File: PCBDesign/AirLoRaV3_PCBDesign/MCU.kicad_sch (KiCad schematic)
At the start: 46 parts, among them IC1 BALFHB-WL-05D3, J2 SMA-J-P-H-ST-EM1, SW1 SW_Push, U3 BGS12WN6E6327, U6 STM32WLE5JCIx, Y1 NX2012SA 32.768KHz

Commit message: Updated Schematic
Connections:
- no-connect marks 27 -> 28
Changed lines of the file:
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@@
+	)
+	(no_connect
+		(at 234.95 154.94)
 	)
 	(no_connect

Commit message: Update circiut
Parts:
- removed J2: SMA-J-P-H-ST-EM1, SMA-J-P-H-ST-EM1:SAMTEC_SMA-J-P-H-ST-EM1, symbol SMA-J-P-H-ST-EM1:SMA-J-P-H-ST-EM1
- added J2: Conn_Coaxial, Connector_Coaxial:U.FL_Molex_MCRF_73412-0110_Vertical, symbol Connector:Conn_Coaxial
- C10: renamed from C8; footprint (none) -> Capacitor_SMD:C_0603_1608Metric
- C11: renamed from C9; footprint (none) -> Capacitor_SMD:C_0603_1608Metric
- C12: renamed from C10; footprint (none) -> Capacitor_SMD:C_0603_1608Metric
- C13: renamed from C11; footprint (none) -> Capacitor_SMD:C_0603_1608Metric
- C14: renamed from C12; footprint (none) -> Capacitor_SMD:C_0603_1608Metric
- C15: renamed from C13; footprint (none) -> Capacitor_SMD:C_0603_1608Metric
- C16, C17, C18, C19, C20, C21, C22, C23, C24, C25, C26, C27, C28, C29, C30, C31, C32, C33, C34, C35, C36, C37, C38, C39, C40: footprint (none) -> Capacitor_SMD:C_0603_1608Metric
- C9: renamed from C7; footprint (none) -> Capacitor_SMD:C_0603_1608Metric
- IC1: footprint BALFHBWL05D3 -> footprint:BALFHBWL05D3
- L2, L4, L5: footprint (none) -> Inductor_SMD:L_0603_1608Metric
- L3: footprint (none) -> Inductor_SMD:L_6.3x6.3_H3
- R7: renamed from R1; footprint (none) -> Resistor_SMD:R_0603_1608Metric
- R8: renamed from R2; footprint (none) -> Resistor_SMD:R_0603_1608Metric
- R9: renamed from R3; footprint (none) -> Resistor_SMD:R_0603_1608Metric
- SW1: footprint (none) -> Button_Switch_SMD:SW_Push_SPST_NO_Alps_SKRK
- U3: footprint Package_LGA:Infineon_PG-TSNP-6-10_0.7x1.1mm_0.7x1.1mm_P0.4mm -> footprint:BGS12SN6E6327XTSA1
- U4: renamed from U6; LCSC (none) -> C1121847; MFR (none) -> STM32WLE5CBU6
- XTAL1: footprint NT2016SA-32M-END4263A_NDK -> footprint:NT2016SA-32M-END4263A_NDK
- Y1: footprint (none) -> footprint:XTAL_NX2012SA-32.768K-STD-MUB-1
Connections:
- net GND: now also J2.1 (In)
- net at C9.2, L2.2: now also J2.2 (Ext)
- net PA6: now reaches U4.F4 (PA6)
- net PA7: now reaches U4.H3 (PA7)
- net PA4: now reaches U4.J1 (PA4)
- net PA5: now reaches U4.J2 (PA5)
- no-connect marks 28 -> 24

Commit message: Update PCB layout
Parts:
- added H1, H2, H3, H4: MountingHole_Pad, MountingHole:MountingHole_3mm_Pad_Via, symbol Mechanical:MountingHole_Pad
- L3: footprint Inductor_SMD:L_6.3x6.3_H3 -> Capacitor_SMD:C_0603_1608Metric_Pad1.08x0.95mm_HandSolder
- SW1: footprint Button_Switch_SMD:SW_Push_SPST_NO_Alps_SKRK -> Button_Switch_SMD:SW_Push_1P1T_NO_Vertical_Wuerth_434133025816
- renumbered R7 to R10, R8 to R11, R9 to R12
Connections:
- net GND: now also J2.2 (Ext), H1.1, H2.1, H3.1, H4.1; no longer J2.1 (In)
- net at C9.2, L2.2: now also J2.1 (In); no longer J2.2 (Ext)
- net PA12: now reaches U4.A9 (PA12)
- net PA11: now reaches U4.B9 (PA11)
- net PB2: now reaches U4.D8 (PB2)
- net PA8: now reaches U4.J3 (PA8)
- no-connect marks 24 -> 20
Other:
- moved on the sheet: J2

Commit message: Update schematic
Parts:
- removed C17: 68pF, Capacitor_SMD:C_0603_1608Metric, symbol Device:C
- removed C23: 47pF, Capacitor_SMD:C_0603_1608Metric, symbol Device:C
- removed C29, C36, C39: 100nF, Capacitor_SMD:C_0603_1608Metric, symbol Device:C
- removed C31, C33: 10pF, Capacitor_SMD:C_0603_1608Metric, symbol Device:C
- removed C35: 4.7uF, Capacitor_SMD:C_0603_1608Metric, symbol Device:C
- removed L5: 1400R 1GHz, Inductor_SMD:L_0603_1608Metric, symbol Device:L
- removed U4: STM32WLE5JCIx, Package_BGA:ST_UFBGA-73_5x5mm_Layout9x9_P0.5mm, symbol MCU_ST_STM32WL:STM32WLE5JCIx
- removed XTAL1: NT2016SA-32M-END4263A, footprint:NT2016SA-32M-END4263A_NDK, symbol NT2016SA-32M-:NT2016SA-32M-END4263A
- added C18: 0.47uF, Capacitor_SMD:C_0603_1608Metric, symbol Device:C
- added C27: 4.7uF, Capacitor_SMD:C_0603_1608Metric, symbol Device:C
- added C28: 100nF, Capacitor_SMD:C_0603_1608Metric, symbol Device:C
- added J3: LED, Connector_JST:JST_XA_B02B-XASK-1-A_1x02_P2.50mm_Vertical, symbol Connector:Conn_01x02_Pin
- added Q1: S8050, Package_TO_SOT_SMD:SOT-23, symbol Transistor_BJT:S8050
- added R13: 1K, Resistor_SMD:R_0603_1608Metric, symbol Device:R
- added U4: STM32WLE5CCUx, Package_DFN_QFN:QFN-48-1EP_7x7mm_P0.5mm_EP5.6x5.6mm, symbol MCU_ST_STM32WL:STM32WLE5CCUx
- added X1: NX2016SA-32MHZ, footprint:NX2016SA_NDK, symbol NX2016SA-32MHZ:NX2016SA-32MHZ-EXS00A-CS06654
- C16: renamed from C32; value 5.1pF -> 6.8pF
- C22: renamed from C34; value 10pF -> 6.8pF
- IC1: value BALFHB-WL-05D3 -> BALFHB-WL-02D3
- R12: value 220 -> 10K
- renumbered C21 to C17, C16 to C19, C18 to C20, C19 to C21, C22 to C23, C26 to C24, C28 to C25, C30 to C26, C20 to C29, C24 to C30, C25 to C31, C27 to C32, C37 to C33, C38 to C34, C40 to C35
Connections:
- net XTA is gone; now on net GND: C22.2
- net +3.3V: now also U4.11 (VDD), U4.37 (VBAT), U4.44 (VDD); no longer C33.1
- net GND: now also C12.1, C14.1, R12.1, C18.2, C27.2, C28.2, Q1.1 (E), U4.48 (VSSSMPS), U4.49 (VSS), X1.2, X1.4; no longer C12.2, C14.2
- net T_SWCLK: now also U4.42 (PA14)
- net T_SWDIO: now also U4.36 (PA13)
- net VDDPA: now also U4.25 (VDDPA); no longer C21.1, C35.1, L3.1
- net at IC1.A2 (RFI_N_OUT): now also U4.21 (RFI_N)
- net at IC1.A3 (RFI_P_OUT): now also U4.20 (RFI_P)
- net at C16.2: now also U4.26 (OSC_IN), X1.1
- net at R11.1: now also U4.38 (PC13)
- net at C23.2, Y1.1: now also U4.40 (PC15)
- net at C19.2, Y1.2: now also U4.39 (PC14)
- net at R10.2, U3.4 (VDD): now also C12.2, C14.2; no longer C12.1, C14.1
- net at C22.1: now also U4.27 (OSC_OUT), X1.3; no longer R12.2
- net at C17.2: now also U4.23 (RFO_HP)
- net at C20.2, SW1.2: now also U4.18 (NRST)
- net at L3.2: now also U4.47 (VLXSMPS)
- net VREF+: no longer names the net of C25.1, C26.1, L4.2
- net VREF+: now also U4.41 (VDDA)
- new net: R12.2, U4.19 (PH3)
- new net: R13.1, U4.8 (PA1)
- new net: J3.1 (Pin_1), Q1.3 (C)
- new net: Q1.2 (B), R13.2
- new net +5V: J3.2 (Pin_2)
- new net SCL1: U4.4 (PB6)
- new net SDA1: U4.5 (PB7)
- new net VDDRF: C27.1, C28.1, C33.1, U4.28 (VDDRF), U4.46 (VDDSMPS)
- new net VDDRF1V55: C18.1, C21.1, C35.1, L3.1, U4.29 (VDDRF1V55), U4.45 (VFBSMPS)
- no-connect marks 20 -> 24
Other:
- note added: "LED"
- moved on the sheet: C10, C11, C12, C13, C14, C15, C16, C17, C19, C22, C23, C25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

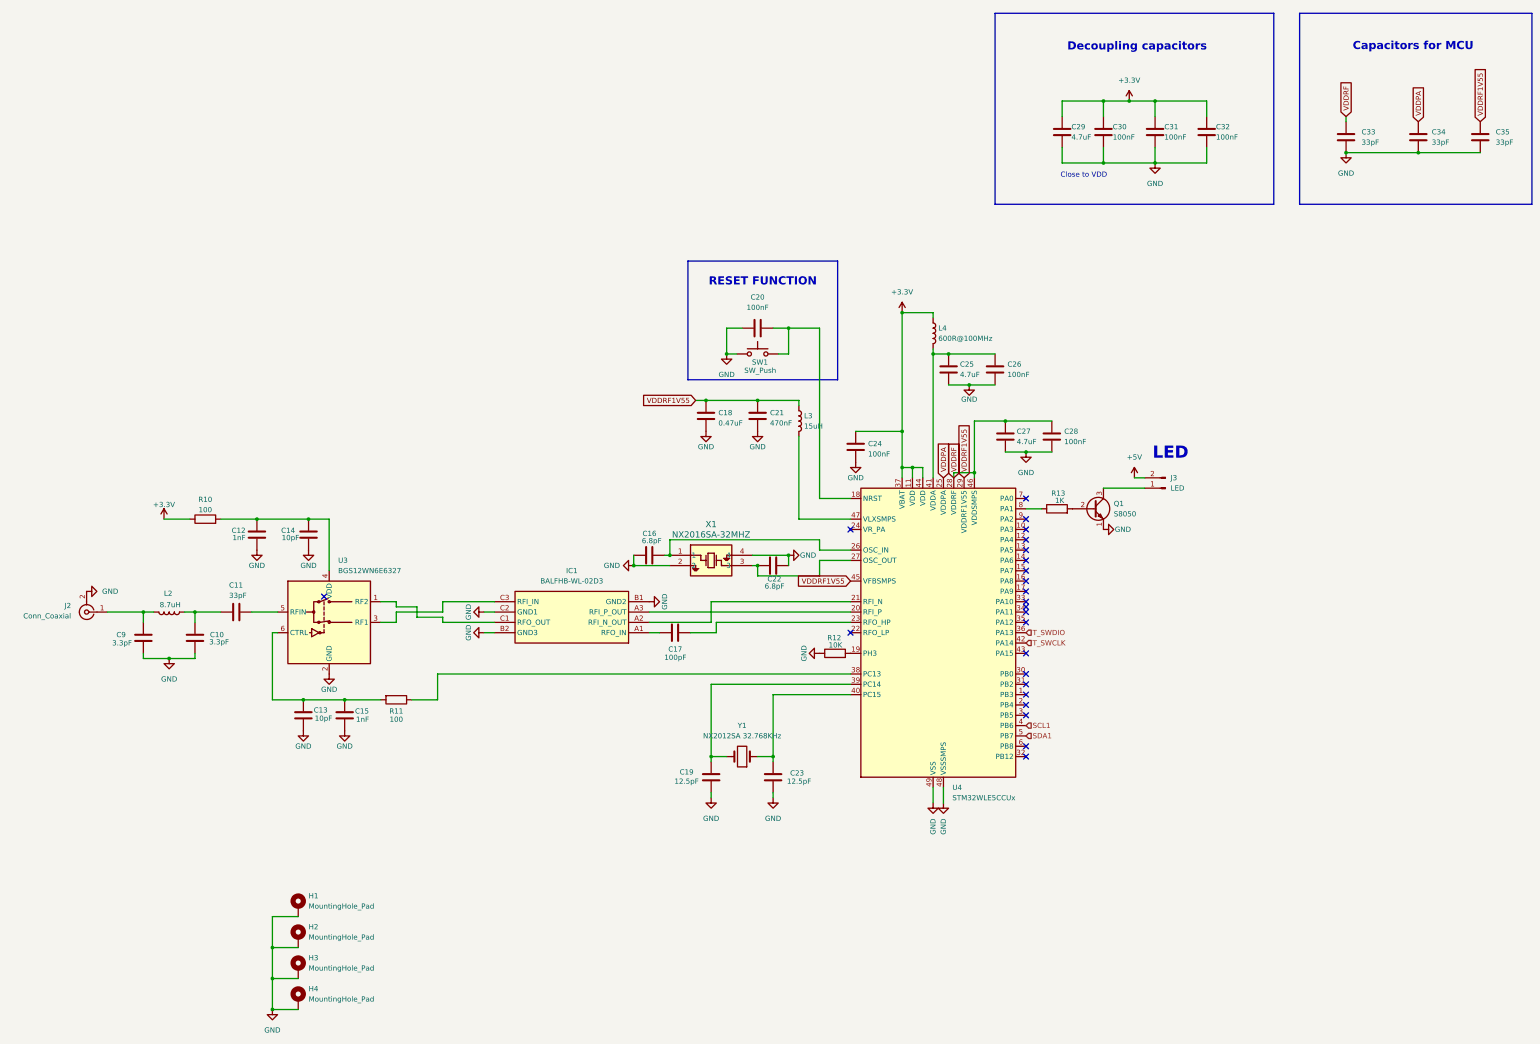
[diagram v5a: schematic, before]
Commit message: Update circuit buck converter and sensor
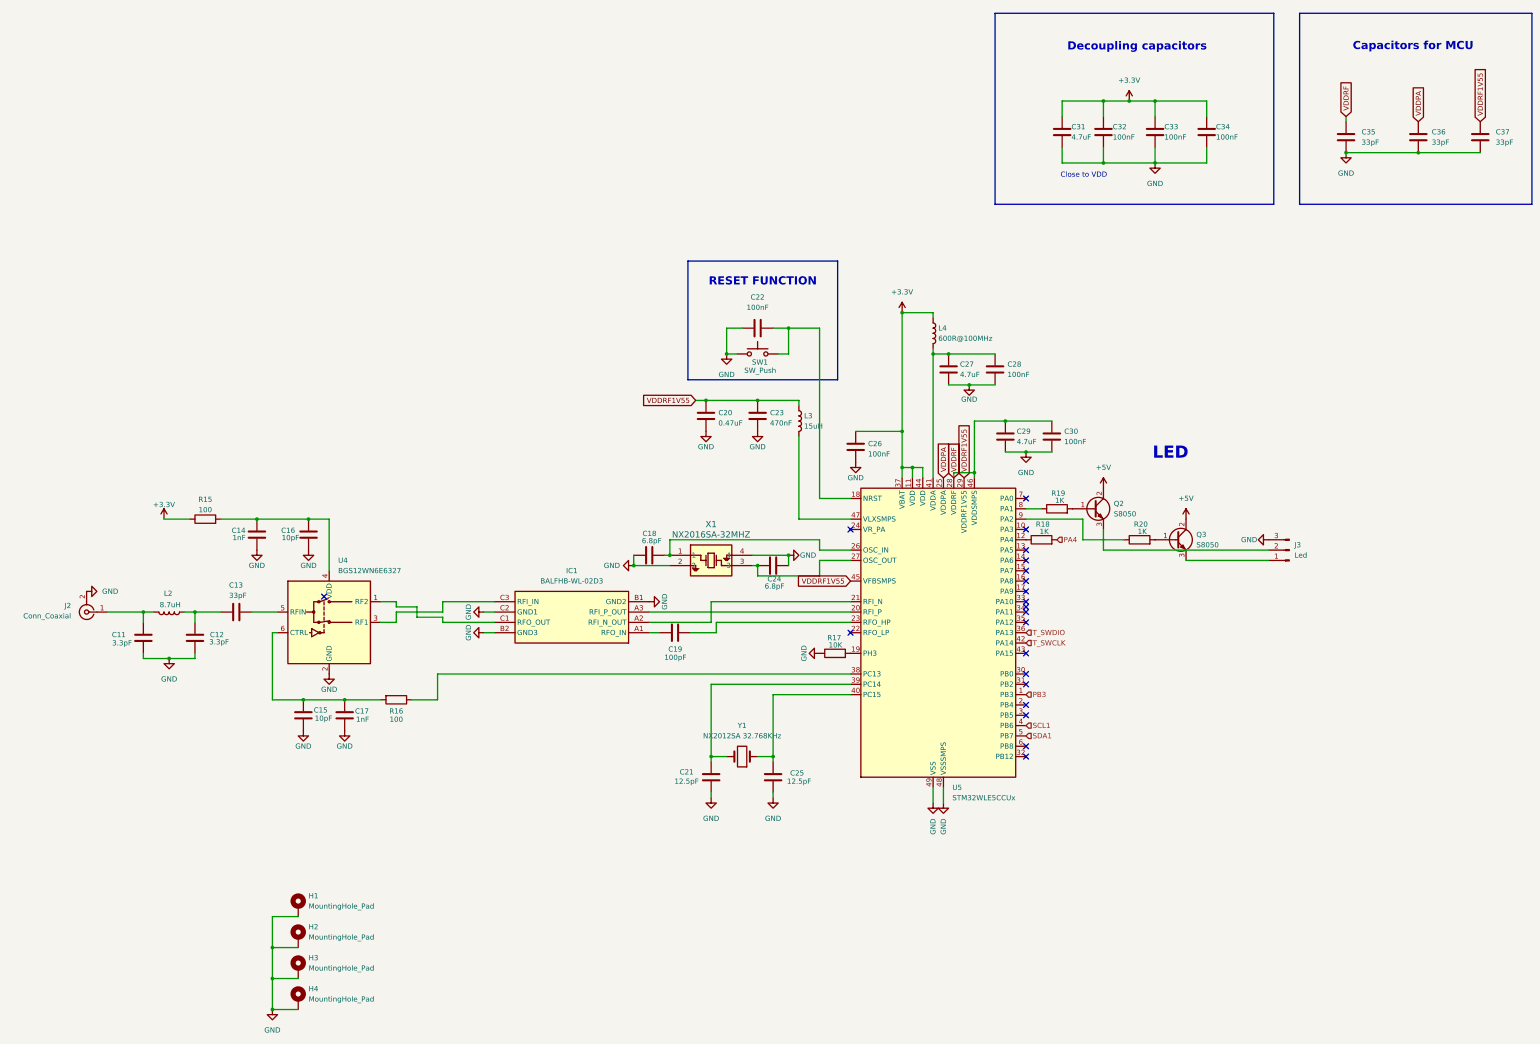
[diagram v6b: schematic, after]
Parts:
- removed J3: LED, Connector_JST:JST_XA_B02B-XASK-1-A_1x02_P2.50mm_Vertical, symbol Connector:Conn_01x02_Pin
- added J3: Led, Connector_Molex:Molex_CLIK-Mate_502585-0370_1x03-1MP_P1.50mm_Horizontal, symbol Connector:Conn_01x03_Pin
- added Q3: S8050, Package_TO_SOT_SMD:SOT-23, symbol Transistor_BJT:S8050
- added R18, R20: 1K, Resistor_SMD:R_0603_1608Metric, symbol Device:R
- renumbered C9 to C11, C10 to C12, C11 to C13, C12 to C14, C13 to C15, C14 to C16, C15 to C17, C16 to C18, C17 to C19, C18 to C20, C19 to C21, C20 to C22, C21 to C23, C22 to C24, C23 to C25, C24 to C26, C25 to C27, C26 to C28, C27 to C29, C28 to C30, C29 to C31, C30 to C32, C31 to C33, C32 to C34, C33 to C35, C34 to C36, C35 to C37, Q1 to Q2, R10 to R15, R11 to R16, R12 to R17, R13 to R19, U3 to U4, U4 to U5
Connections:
- net +5V: now also Q2.2 (C), Q3.2 (C)
- net GND: now also J3.3 (Pin_3); no longer Q2.1 (E)
- net PB3: now reaches U5.1 (PB3)
- net at U5.12 (PA4): now also R18.1
- net at U5.9 (PA2): now also R20.1
- net at Q2.3 (E): now also J3.2 (Pin_2)
- net at R19.2: now also Q2.1 (B); no longer Q2.2 (B)
- new net: Q3.1 (B), R20.2
- new net: J3.1 (Pin_1), Q3.3 (E)
- new net PA4: R18.2
- no-connect marks 24 -> 21

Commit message: Update schematic
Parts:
- J3: footprint Connector_Molex:Molex_CLIK-Mate_502585-0370_1x03-1MP_P1.50mm_Horizontal -> Connector_JST:JST_XH_B3B-XH-A_1x03_P2.50mm_Vertical
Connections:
- net SCL2: now reaches U5.34 (PA11)
- net SDA2: now reaches U5.35 (PA12)
- net SCL1: no longer names the net of U5.4 (PB6)
- net SDA1: no longer names the net of U5.5 (PB7)
- no-connect marks 21 -> 18
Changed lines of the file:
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@@
 	)
 	(no_connect
-		(at 278.13 167.64)
-	)
-	(no_connect
 		(at 278.13 198.12)
 	)
@@
 	)
 	(no_connect
-		(at 278.13 163.83)
-	)
-	(no_connect
 		(at 278.13 180.34)
 	)
@@
 	)
 	(no_connect
-		(at 278.13 165.1)
-	)
-	(no_connect
 		(at 278.13 144.78)
 	)
@@
 		)
 	)
-	(hierarchical_label "SDA1"
+	(hierarchical_label "SDA2"
 		(shape input)
-		(at 278.13 195.58 0)
+		(at 278.13 167.64 0)
 		(fields_autoplaced yes)
 		(effects
@@
 		)
 	)
-	(hierarchical_label "SCL1"
+	(hierarchical_label "SCL2"
 		(shape input)
-		(at 278.13 193.04 0)
+		(at 278.13 165.1 0)
 		(fields_autoplaced yes)
 		(effects
@@
 			)
 		)
-		(property "Footprint" "Connector_Molex:Molex_CLIK-Mate_502585-0370_1x03-1MP_P1.50mm_Horizontal"
+		(property "Footprint" "Connector_JST:JST_XH_B3B-XH-A_1x03_P2.50mm_Vertical"
 			(at 342.9 149.86 0)
 			(effects

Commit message: Update PCB
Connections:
- net at R20.1: now also U5.14 (PA6); no longer U5.9 (PA2)
- net PA3: now reaches U5.10 (PA3)
- net at U5.13 (PA5): now also R19.1
- net at U5.8 (PA1): no longer R19.1
- net PB3: no longer names the net of U5.1 (PB3)
- no-connect marks 18 -> 20
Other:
- moved on the sheet: J3, Q2, Q3, R19, R20
